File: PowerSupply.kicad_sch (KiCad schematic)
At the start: 40 parts

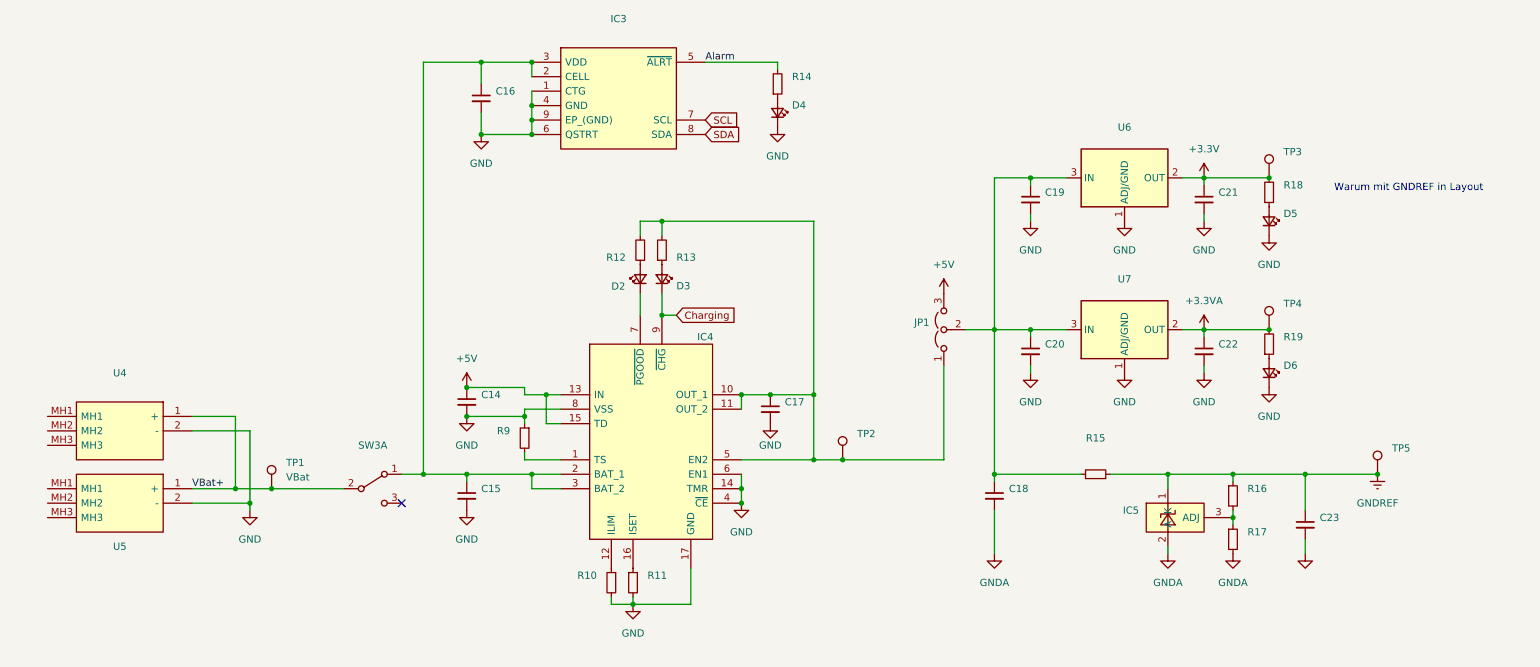
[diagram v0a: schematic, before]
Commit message: small fix for jlcpcb parts detection
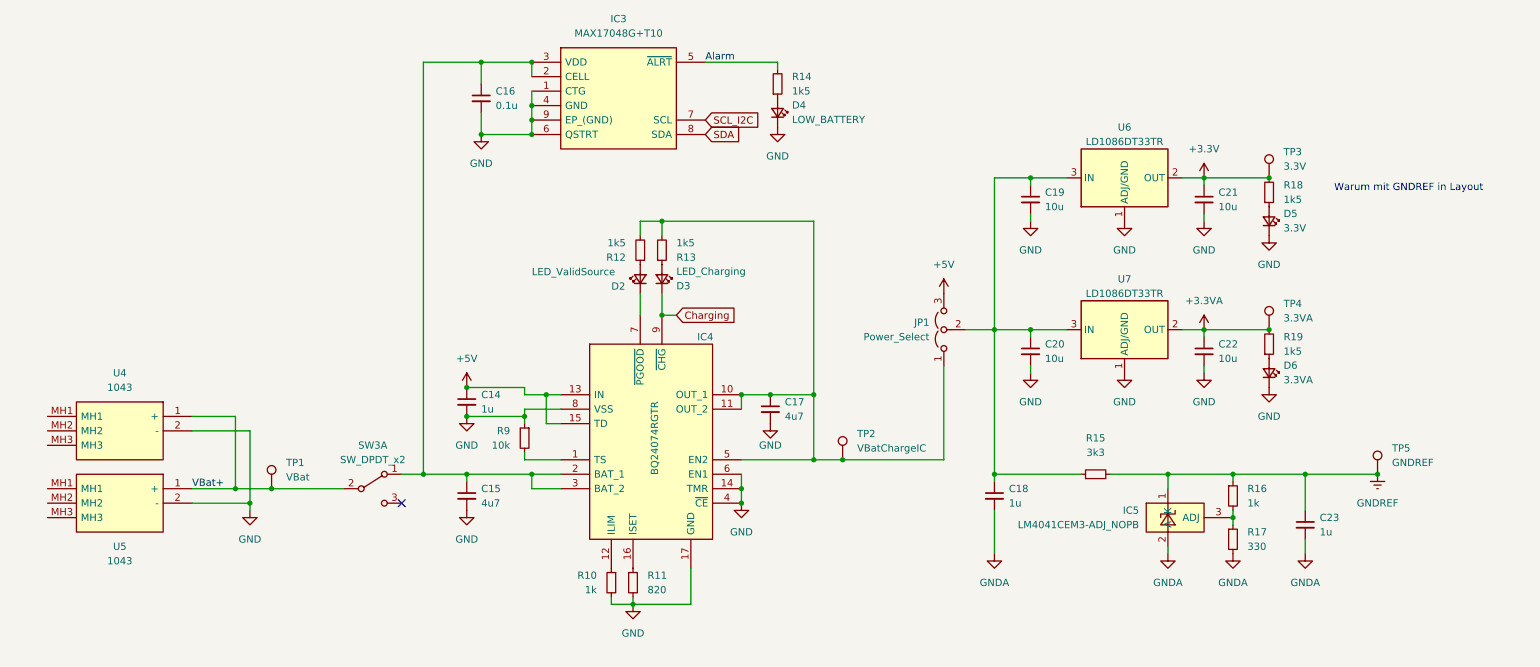
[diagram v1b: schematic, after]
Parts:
- C14, C18, C23: value (none) -> 1u; footprint (none) -> Capacitor_SMD:C_0805_2012Metric_Pad1.18x1.45mm_HandSolder
- C15, C17: value (none) -> 4u7; footprint (none) -> Capacitor_SMD:C_0805_2012Metric_Pad1.18x1.45mm_HandSolder
- C16: value (none) -> 0.1u; footprint (none) -> Capacitor_SMD:C_0805_2012Metric_Pad1.18x1.45mm_HandSolder
- C19, C20, C21, C22: value (none) -> 10u; footprint (none) -> Capacitor_SMD:C_0805_2012Metric_Pad1.18x1.45mm_HandSolder
- D2: value (none) -> LED_ValidSource; footprint (none) -> LED_SMD:LED_0805_2012Metric_Pad1.15x1.40mm_HandSolder
- D3: value (none) -> LED_Charging; footprint (none) -> LED_SMD:LED_0805_2012Metric_Pad1.15x1.40mm_HandSolder
- D4: value (none) -> LOW_BATTERY; footprint (none) -> LED_SMD:LED_0805_2012Metric_Pad1.15x1.40mm_HandSolder
- D5: value (none) -> 3.3V; footprint (none) -> LED_SMD:LED_0805_2012Metric_Pad1.15x1.40mm_HandSolder
- D6: value (none) -> 3.3VA; footprint (none) -> LED_SMD:LED_0805_2012Metric_Pad1.15x1.40mm_HandSolder
- IC3: value (none) -> MAX17048G+T10
- IC4: value (none) -> BQ24074RGTR
- IC5: value (none) -> LM4041CEM3-ADJ_NOPB
- JP1: value (none) -> Power_Select; footprint (none) -> Connector_PinHeader_2.54mm:PinHeader_1x03_P2.54mm_Vertical
- R10, R16: value (none) -> 1k; footprint (none) -> Resistor_SMD:R_0805_2012Metric_Pad1.20x1.40mm_HandSolder
- R11: value (none) -> 820; footprint (none) -> Resistor_SMD:R_0805_2012Metric_Pad1.20x1.40mm_HandSolder
- R12, R13, R14, R18, R19: value (none) -> 1k5; footprint (none) -> Resistor_SMD:R_0805_2012Metric_Pad1.20x1.40mm_HandSolder
- R15: value (none) -> 3k3; footprint (none) -> Resistor_SMD:R_0805_2012Metric_Pad1.20x1.40mm_HandSolder
- R17: value (none) -> 330; footprint (none) -> Resistor_SMD:R_0805_2012Metric_Pad1.20x1.40mm_HandSolder
- R9: value (none) -> 10k; footprint (none) -> Resistor_SMD:R_0805_2012Metric_Pad1.20x1.40mm_HandSolder
- SW3: value (none) -> SW_DPDT_x2; footprint (none) -> project_library:25136NAH6
- TP2: value (none) -> VBatChargeIC; footprint (none) -> TestPoint:TestPoint_Keystone_5000-5004_Miniature
- TP3: value (none) -> 3.3V; footprint (none) -> TestPoint:TestPoint_Keystone_5000-5004_Miniature
- TP4: value (none) -> 3.3VA; footprint (none) -> TestPoint:TestPoint_Keystone_5000-5004_Miniature
- TP5: value (none) -> GNDREF; footprint (none) -> TestPoint:TestPoint_Keystone_5000-5004_Miniature
- U4, U5: value (none) -> 1043
- U6, U7: value (none) -> LD1086DT33TR
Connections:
- net SCL renamed SCL_I2C

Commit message: Added ADC vor Trigger and changed Layout
Some Traces cant be good routed
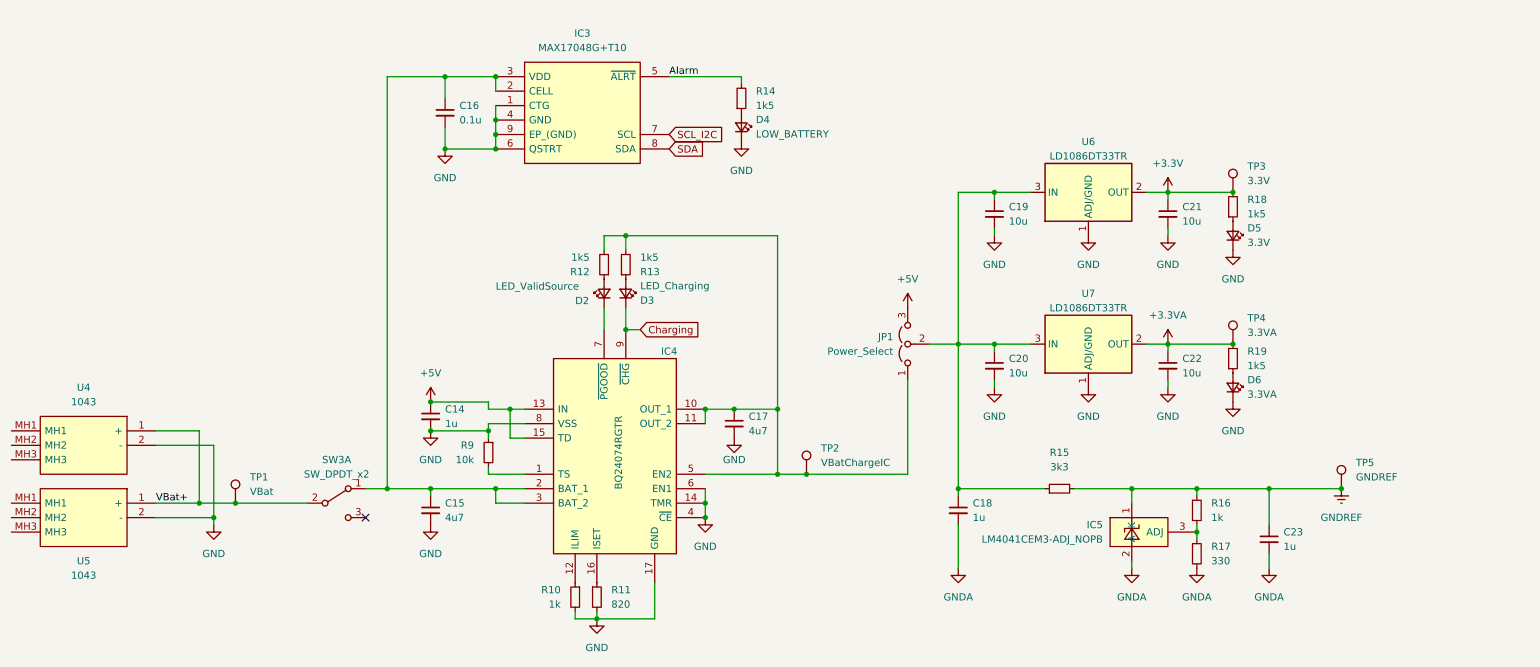
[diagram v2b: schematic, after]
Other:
- note removed: "Warum mit GNDREF in Layout"
- moved on the sheet: C14, C15, C16, C17, C18, C19, C20, C21, C22, C23, D2, D3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

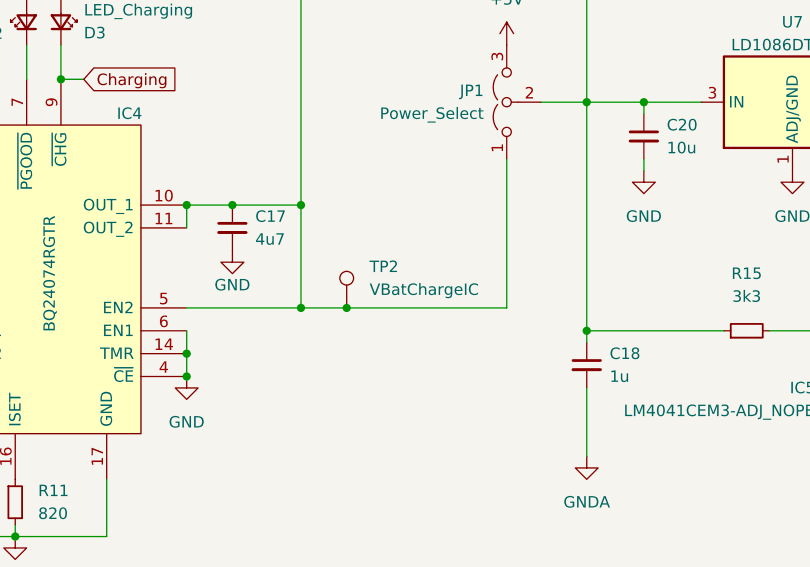
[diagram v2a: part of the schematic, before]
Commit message: new idear to arange gnd ref in layout
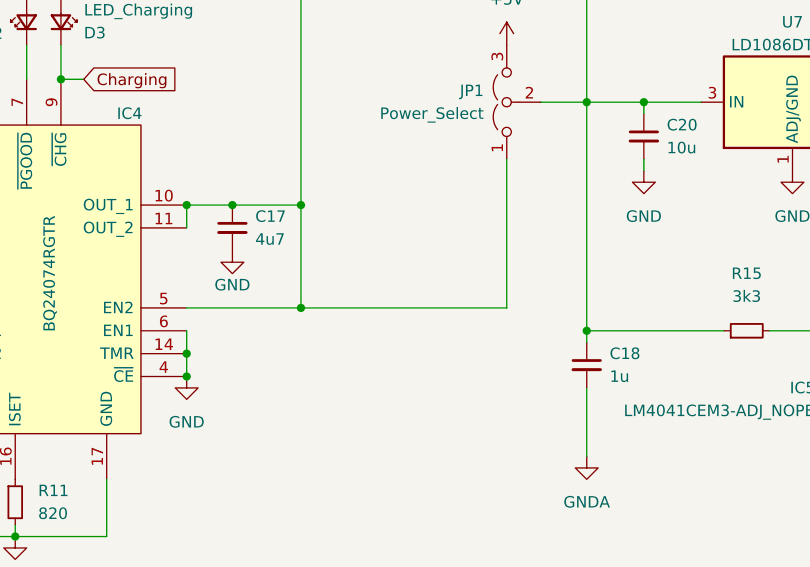
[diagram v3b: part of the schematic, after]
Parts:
- removed TP2: VBatChargeIC, TestPoint:TestPoint_Keystone_5000-5004_Miniature, symbol Connector:TestPoint
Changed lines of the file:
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@@
   (junction (at 163.83 100.33) (diameter 0) (color 0 0 0 0)
-  )
-  (junction (at 168.91 111.76) (diameter 0) (color 0 0 0 0)
   )
   (junction (at 232.41 88.9) (diameter 0) (color 0 0 0 0)
@@
     (stroke (width 0) (type default) (color 0 0 0 0))
   )
-  (wire (pts (xy 168.91 111.76) (xy 186.69 111.76))
-    (stroke (width 0) (type default) (color 0 0 0 0))
-  )
   (wire (pts (xy 186.69 111.76) (xy 186.69 95.25))
     (stroke (width 0) (type default) (color 0 0 0 0))
@@
     (stroke (width 0) (type default) (color 0 0 0 0))
   )
-  (wire (pts (xy 163.83 111.76) (xy 168.91 111.76))
+  (wire (pts (xy 163.83 111.76) (xy 186.69 111.76))
     (stroke (width 0) (type default) (color 0 0 0 0))
   )
@@
       (effects (font (size 1.27 1.27)) hide)
     )
-    (pin "1")
-  )
-  (symbol (lib_id "Connector:TestPoint") (at 168.91 111.76 0) (unit 1)
-    (in_bom yes) (on_board yes) (fields_autoplaced)
-    (property "Reference" "TP2" (id 0) (at 171.45 107.1879 0)
-      (effects (font (size 1.27 1.27)) (justify left))
-    )
-    (property "Value" "VBatChargeIC" (id 1) (at 171.45 109.7279 0)
-      (effects (font (size 1.27 1.27)) (justify left))
-    )
-    (property "Footprint" "TestPoint:TestPoint_Keystone_5000-5004_Miniature" (id 2) (at 173.99 111.76 0)
-      (effects (font (size 1.27 1.27)) hide)
-    )
-    (property "Datasheet" "~" (id 3) (at 173.99 111.76 0)
-      (effects (font (size 1.27 1.27)) hide)
-    )

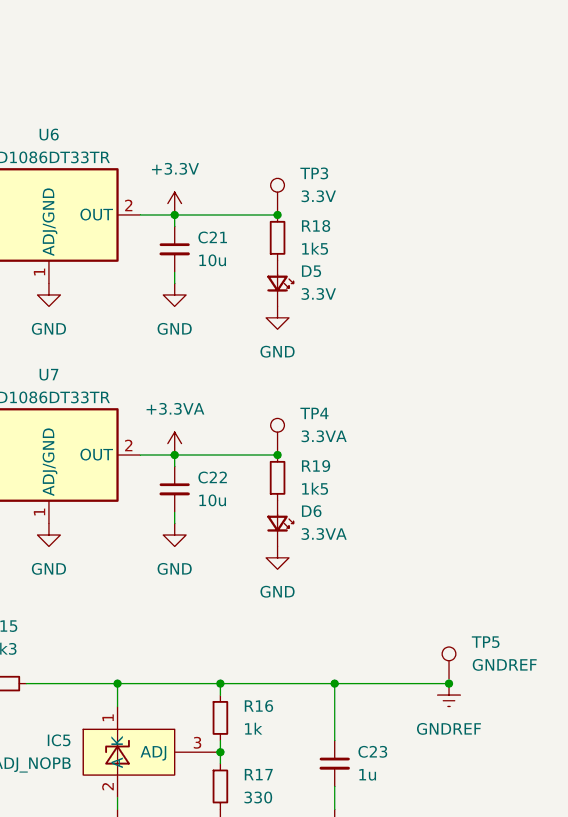
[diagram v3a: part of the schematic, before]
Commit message: added values for analog front end
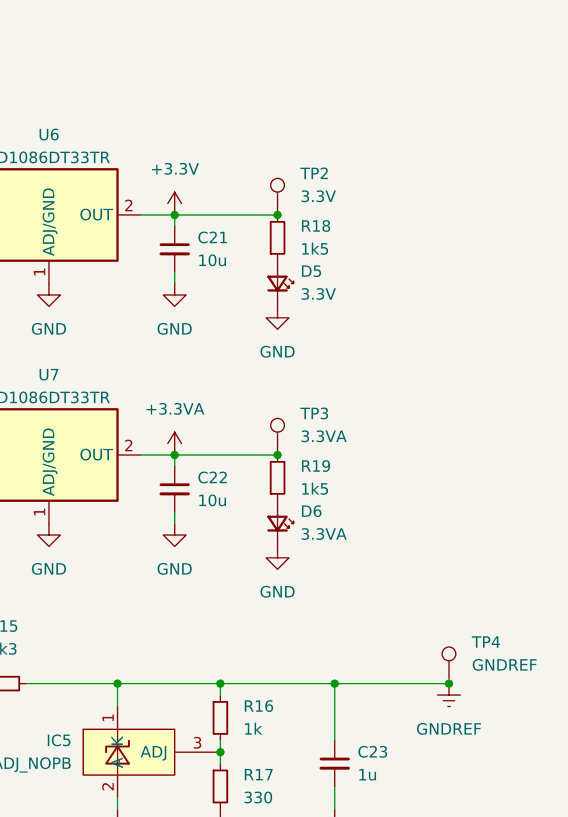
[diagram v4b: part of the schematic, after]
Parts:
- renumbered TP3 to TP2, TP4 to TP3, TP5 to TP4
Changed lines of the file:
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@@
   (symbol (lib_id "Connector:TestPoint") (at 243.84 62.23 0) (unit 1)
     (in_bom yes) (on_board yes) (fields_autoplaced)
-    (property "Reference" "TP3" (id 0) (at 246.38 57.6579 0)
+    (property "Reference" "TP2" (id 0) (at 246.38 57.6579 0)
       (effects (font (size 1.27 1.27)) (justify left))
     )
@@
   (symbol (lib_id "Connector:TestPoint") (at 243.84 88.9 0) (unit 1)
     (in_bom yes) (on_board yes) (fields_autoplaced)
-    (property "Reference" "TP4" (id 0) (at 246.38 84.3279 0)
+    (property "Reference" "TP3" (id 0) (at 246.38 84.3279 0)
       (effects (font (size 1.27 1.27)) (justify left))
     )
@@
   (symbol (lib_id "Connector:TestPoint") (at 262.89 114.3 0) (unit 1)
     (in_bom yes) (on_board yes) (fields_autoplaced)
-    (property "Reference" "TP5" (id 0) (at 265.43 109.7279 0)
-      (effects (font (size 1.27 1.27)) (justify left))
-    )
+    (property "Reference" "TP4" (id 0) (at 265.43 109.7279 0)
+      (effects (font (size 1.27 1.27)) (justify left))
+    )

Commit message: updated circuit
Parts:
- removed C18, C23: 1u, Capacitor_SMD:C_0805_2012Metric_Pad1.18x1.45mm_HandSolder, symbol Device:C_Small
- removed IC5: LM4041CEM3-ADJ_NOPB, project_library:LM4041CEM3-ADJ_NOPB, symbol project_library:LM4041CEM3-ADJ_NOPB
- removed R15: 3k3, Resistor_SMD:R_0805_2012Metric_Pad1.20x1.40mm_HandSolder, symbol Device:R_Small
- removed R16: 1k, Resistor_SMD:R_0805_2012Metric_Pad1.20x1.40mm_HandSolder, symbol Device:R_Small
- removed R17: 330, Resistor_SMD:R_0805_2012Metric_Pad1.20x1.40mm_HandSolder, symbol Device:R_Small
- removed TP4: GNDREF, TestPoint:TestPoint_Keystone_5000-5004_Miniature, symbol Connector:TestPoint

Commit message: routing
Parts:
- C14: value 1u -> (none); footprint Capacitor_SMD:C_0805_2012Metric_Pad1.18x1.45mm_HandSolder -> (none)
- C15, C17: value 4u7 -> (none); footprint Capacitor_SMD:C_0805_2012Metric_Pad1.18x1.45mm_HandSolder -> (none)
- C16: value 0.1u -> (none); footprint Capacitor_SMD:C_0805_2012Metric_Pad1.18x1.45mm_HandSolder -> (none)
- D4: value LOW_BATTERY -> (none); footprint LED_SMD:LED_0805_2012Metric_Pad1.15x1.40mm_HandSolder -> (none)
- R10: value 1k -> (none); footprint Resistor_SMD:R_0805_2012Metric_Pad1.20x1.40mm_HandSolder -> (none)
- R11: value 820 -> (none); footprint Resistor_SMD:R_0805_2012Metric_Pad1.20x1.40mm_HandSolder -> (none)
- R14: value 1k5 -> (none); footprint Resistor_SMD:R_0805_2012Metric_Pad1.20x1.40mm_HandSolder -> (none)
- R9: value 10k -> (none); footprint Resistor_SMD:R_0805_2012Metric_Pad1.20x1.40mm_HandSolder -> (none)
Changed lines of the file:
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@@
       (effects (font (size 1.27 1.27)) (justify left))
     )
-    (property "Value" "4u7" (id 1) (at 158.75 104.1462 0)
-      (effects (font (size 1.27 1.27)) (justify left))
-    )
-    (property "Footprint" "Capacitor_SMD:C_0805_2012Metric_Pad1.18x1.45mm_HandSolder" (id 2) (at 156.21 102.87 0)
+    (property "Value" "" (id 1) (at 158.75 104.1462 0)
+      (effects (font (size 1.27 1.27)) (justify left))
+    )
+    (property "Footprint" "" (id 2) (at 156.21 102.87 0)
       (effects (font (size 1.27 1.27)) hide)
     )
@@
       (effects (font (size 1.27 1.27)) (justify left))
     )
-    (property "Value" "820" (id 1) (at 134.62 134.62 0)
-      (effects (font (size 1.27 1.27)) (justify left))
-    )
-    (property "Footprint" "Resistor_SMD:R_0805_2012Metric_Pad1.20x1.40mm_HandSolder" (id 2) (at 132.08 133.35 0)
+    (property "Value" "" (id 1) (at 134.62 134.62 0)
+      (effects (font (size 1.27 1.27)) (justify left))
+    )
+    (property "Footprint" "" (id 2) (at 132.08 133.35 0)
       (effects (font (size 1.27 1.27)) hide)
     )
@@
       (effects (font (size 1.27 1.27)) (justify left))
     )
-    (property "Value" "4u7" (id 1) (at 105.41 119.3862 0)
-      (effects (font (size 1.27 1.27)) (justify left))
-    )
-    (property "Footprint" "Capacitor_SMD:C_0805_2012Metric_Pad1.18x1.45mm_HandSolder" (id 2) (at 102.87 118.11 0)
+    (property "Value" "" (id 1) (at 105.41 119.3862 0)
+      (effects (font (size 1.27 1.27)) (justify left))
+    )
+    (property "Footprint" "" (id 2) (at 102.87 118.11 0)
       (effects (font (size 1.27 1.27)) hide)
     )
@@
       (effects (font (size 1.27 1.27)) (justify left))
     )
-    (property "Value" "1k5" (id 1) (at 160.02 46.99 0)
-      (effects (font (size 1.27 1.27)) (justify left))
-    )
-    (property "Footprint" "Resistor_SMD:R_0805_2012Metric_Pad1.20x1.40mm_HandSolder" (id 2) (at 157.48 45.72 0)
+    (property "Value" "" (id 1) (at 160.02 46.99 0)
+      (effects (font (size 1.27 1.27)) (justify left))
+    )
+    (property "Footprint" "" (id 2) (at 157.48 45.72 0)
       (effects (font (size 1.27 1.27)) hide)
     )
@@
       (effects (font (size 1.27 1.27)) (justify left))
     )
-    (property "Value" "1u" (id 1) (at 105.41 102.8762 0)
-      (effects (font (size 1.27 1.27)) (justify left))
-    )
-    (property "Footprint" "Capacitor_SMD:C_0805_2012Metric_Pad1.18x1.45mm_HandSolder" (id 2) (at 102.87 101.6 0)
+    (property "Value" "" (id 1) (at 105.41 102.8762 0)
+      (effects (font (size 1.27 1.27)) (justify left))
+    )
+    (property "Footprint" "" (id 2) (at 102.87 101.6 0)
       (effects (font (size 1.27 1.27)) hide)
     )
@@
       (effects (font (size 1.27 1.27)) (justify left))
     )
-    (property "Value" "1k" (id 1) (at 125.73 134.62 0)
-      (effects (font (size 1.27 1.27)) (justify left))
-    )
-    (property "Footprint" "Resistor_SMD:R_0805_2012Metric_Pad1.20x1.40mm_HandSolder" (id 2) (at 128.27 133.35 0)
+    (property "Value" "" (id 1) (at 125.73 134.62 0)
+      (effects (font (size 1.27 1.27)) (justify left))
+    )
+    (property "Footprint" "" (id 2) (at 128.27 133.35 0)
       (effects (font (size 1.27 1.27)) hide)
     )
@@
       (effects (font (size 1.27 1.27)) (justify left))
     )
-    (property "Value" "0.1u" (id 1) (at 107.95 49.5362 0)
-      (effects (font (size 1.27 1.27)) (justify left))
-    )
-    (property "Footprint" "Capacitor_SMD:C_0805_2012Metric_Pad1.18x1.45mm_HandSolder" (id 2) (at 105.41 48.26 0)
+    (property "Value" "" (id 1) (at 107.95 49.5362 0)
+      (effects (font (size 1.27 1.27)) (justify left))
+    )
+    (property "Footprint" "" (id 2) (at 105.41 48.26 0)
       (effects (font (size 1.27 1.27)) hide)
     )
@@
       (effects (font (size 1.27 1.27)) (justify left))
     )
-    (property "Value" "10k" (id 1) (at 110.49 109.22 0)
-      (effects (font (size 1.27 1.27)) (justify left))
-    )
-    (property "Footprint" "Resistor_SMD:R_0805_2012Metric_Pad1.20x1.40mm_HandSolder" (id 2) (at 113.03 107.95 0)
+    (property "Value" "" (id 1) (at 110.49 109.22 0)
+      (effects (font (size 1.27 1.27)) (justify left))
+    )
+    (property "Footprint" "" (id 2) (at 113.03 107.95 0)
       (effects (font (size 1.27 1.27)) hide)
     )
@@
       (effects (font (size 1.27 1.27)) (justify left))
     )
-    (property "Value" "LOW_BATTERY" (id 1) (at 160.02 52.0064 90)
-      (effects (font (size 1.27 1.27)) (justify left))
-    )
-    (property "Footprint" "LED_SMD:LED_0805_2012Metric_Pad1.15x1.40mm_HandSolder" (id 2) (at 157.48 50.8 90)
-      (effects (font (size 1.27 1.27)) hide)
-    )
+    (property "Value" "" (id 1) (at 160.02 52.0064 90)
+      (effects (font (size 1.27 1.27)) (justify left))
+    )
+    (property "Footprint" "" (id 2) (at 157.48 50.8 90)
+      (effects (font (size 1.27 1.27)) hide)
+    )
